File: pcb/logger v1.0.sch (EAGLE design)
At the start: 29 parts, among them J1 MICRO-SDCARD-CONNECTOR-330006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, K1 RESET, U1 DS1307ZN-1900100P1, U2 CJ1117-3.3-1310190P1, U3 74VHCT125PW, X1 32.768KHZ

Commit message: Mostly wired up
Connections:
- new net AREF: JP2.1, U$4.AREF
- new net D2: JP4.3, U$4.D2
- new net D3: JP4.4, U$4.*D3
- new net D4: JP4.5, U$4.D4
- new net D5: JP4.6, U$4.*D5
- new net D6: JP4.7, U$4.*D6
- new net D7: JP4.8, U$4.D7
- new net D8: JP2.8, U$4.D8
- new net D9: JP2.7, U$4.*D9
- new net N$55: U$4.SCL
- new net N$87: U$4.SDA
- new net RX: JP4.1, U$4.RX
- new net TX: JP4.2, U$4.TX
- net +3V3: now also U$4.3.3V
- net +5V: now also U$4.5V
- net GND: now also U$4.GND@0, U$4.GND@1, U$4.GND@2
- net MISO: now also U$4.D12
- net MOSI: now also U$4.*D11
- net RESET: now also U$4.RES
- net SCK: now also U$4.D13
- net SD_CS: now also U$4.*D10
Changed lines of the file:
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@@
 </variantdefs>
 <classes>
-<class number="0" name="default" width="0" drill="0">
+<class number="0" name="default" width="0.1524" drill="0.3302">
+</class>
+<class number="1" name="3V3" width="0.3048" drill="0.3302">
+<clearance class="0" value="0.1524"/>
+</class>
+<class number="2" name="5V" width="0.3048" drill="0.3302">
+<clearance class="0" value="0.1524"/>
+<clearance class="1" value="0.1524"/>
+</class>
+<class number="3" name="GND" width="0.1524" drill="0.3302">
+<clearance class="0" value="0.1524"/>
+<clearance class="1" value="0.1524"/>
+<clearance class="2" value="0.1524"/>
 </class>
 </classes>
@@
 </busses>
 <nets>
-<net name="+5V" class="0">
+<net name="+5V" class="2">
 <segment>
 <wire x1="53.34" y1="53.34" x2="53.34" y2="63.5" width="0.1524" layer="91"/>
@@
 <pinref part="P+2" gate="1" pin="+5V"/>
 <wire x1="43.18" y1="22.86" x2="44.45" y2="22.86" width="0.1524" layer="91"/>
-<junction x="45.72" y="22.86"/>
 <pinref part="U2" gate="U" pin="IN"/>
-<wire x1="44.45" y1="22.86" x2="45.72" y2="22.86" width="0.1524" layer="91"/>
-<junction x="44.45" y="22.86"/>
 </segment>
 <segment>
@@
 <pinref part="R8" gate="R" pin="2"/>
 </segment>
-</net>
-<net name="GND" class="0">
+<segment>
+<pinref part="U$4" gate="G$1" pin="5V"/>
+<wire x1="66.04" y1="83.82" x2="66.04" y2="76.2" width="0.1524" layer="91"/>
+<label x="66.04" y="76.2" size="1.778" layer="95" rot="R90"/>
+</segment>
+</net>
+<net name="GND" class="3">
 <segment>
 <wire x1="55.88" y1="55.88" x2="58.42" y2="55.88" width="0.1524" layer="91"/>
@@
 <pinref part="GND7" gate="1" pin="GND"/>
 <pinref part="JP2" gate="G$1" pin="2"/>
+<wire x1="40.64" y1="129.54" x2="40.64" y2="119.38" width="0.1524" layer="91"/>
+<junction x="40.64" y="129.54"/>
 </segment>
 <segment>
@@
 <pinref part="GND13" gate="1" pin="GND"/>
 <wire x1="147.32" y1="109.22" x2="147.32" y2="119.38" width="0.1524" layer="91"/>
+</segment>
+<segment>
+<pinref part="U$4" gate="G$1" pin="GND@2"/>
+<wire x1="73.66" y1="83.82" x2="73.66" y2="78.74" width="0.1524" layer="91"/>
+<pinref part="U$4" gate="G$1" pin="GND@0"/>
+<wire x1="78.74" y1="83.82" x2="78.74" y2="78.74" width="0.1524" layer="91"/>
+<wire x1="73.66" y1="78.74" x2="76.2" y2="78.74" width="0.1524" layer="91"/>
+<pinref part="U$4" gate="G$1" pin="GND@1"/>
+<wire x1="76.2" y1="78.74" x2="78.74" y2="78.74" width="0.1524" layer="91"/>
+<wire x1="76.2" y1="83.82" x2="76.2" y2="78.74" width="0.1524" layer="91"/>
+<junction x="76.2" y="78.74"/>
+<label x="73.66" y="76.2" size="1.778" layer="95"/>
 </segment>
 </net>
@@
 <pinref part="K1" gate="G$1" pin="A1"/>
 </segment>
-</net>
-<net name="+3V3" class="0">
+<segment>
+<pinref part="U$4" gate="G$1" pin="RES"/>
+<wire x1="60.96" y1="83.82" x2="60.96" y2="76.2" width="0.1524" layer="91"/>
+<label x="60.96" y="76.2" size="1.778" layer="95" rot="R90"/>
+</segment>
+</net>
+<net name="+3V3" class="1">
 <segment>
 <pinref part="JP12" gate="A" pin="1"/>
@@
 <pinref part="+3V2" gate="G$1" pin="+3V3"/>
 </segment>
+<segment>
+<pinref part="U$4" gate="G$1" pin="3.3V"/>
+<wire x1="68.58" y1="83.82" x2="68.58" y2="76.2" width="0.1524" layer="91"/>
+<label x="68.58" y="76.2" size="1.778" layer="95" rot="R90"/>
+</segment>
 </net>
 <net name="MOSI" class="0">
@@
 <pinref part="ICSP" gate="A" pin="4"/>
 <pinref part="JP2" gate="G$1" pin="5"/>
+<wire x1="48.26" y1="129.54" x2="48.26" y2="119.38" width="0.1524" layer="91"/>
+<junction x="48.26" y="129.54"/>
 </segment>
 <segment>
@@
 <label x="195.58" y="101.6" size="1.778" layer="95"/>
 <pinref part="JP1" gate="A" pin="2"/>
+</segment>
+<segment>
+<pinref part="U$4" gate="G$1" pin="*D11"/>
+<wire x1="68.58" y1="109.22" x2="68.58" y2="114.3" width="0.1524" layer="91"/>
 </segment>
 </net>
@@
 <pinref part="ICSP" gate="A" pin="1"/>
 <pinref part="JP2" gate="G$1" pin="4"/>
+<wire x1="45.72" y1="129.54" x2="45.72" y2="119.38" width="0.1524" layer="91"/>
+<junction x="45.72" y="129.54"/>
 </segment>
 <segment>
@@
 <wire x1="124.46" y1="88.9" x2="134.62" y2="88.9" width="0.1524" layer="91"/>
 <wire x1="134.62" y1="88.9" x2="134.62" y2="93.98" width="0.1524" layer="91"/>
+</segment>
+<segment>
+<pinref part="U$4" gate="G$1" pin="D12"/>
+<wire x1="71.12" y1="109.22" x2="71.12" y2="114.3" width="0.1524" layer="91"/>
 </segment>
 </net>
@@
 <pinref part="ICSP" gate="A" pin="3"/>
 <pinref part="JP2" gate="G$1" pin="3"/>
+<wire x1="43.18" y1="129.54" x2="43.18" y2="119.38" width="0.1524" layer="91"/>
+<junction x="43.18" y="129.54"/>
 </segment>
 <segment>
@@
 <label x="195.58" y="96.52" size="1.778" layer="95"/>
 <pinref part="JP1" gate="A" pin="4"/>
+</segment>
+<segment>
+<pinref part="U$4" gate="G$1" pin="D13"/>
+<wire x1="73.66" y1="109.22" x2="73.66" y2="114.3" width="0.1524" layer="91"/>
 </segment>
 </net>
@@
 <label x="60.96" y="144.78" size="1.778" layer="95" rot="MR0"/>
 <pinref part="JP2" gate="G$1" pin="6"/>
+<wire x1="50.8" y1="129.54" x2="50.8" y2="119.38" width="0.1524" layer="91"/>
+<junction x="50.8" y="129.54"/>
+</segment>
+<segment>
+<pinref part="U$4" gate="G$1" pin="*D10"/>
+<wire x1="66.04" y1="109.22" x2="66.04" y2="114.3" width="0.1524" layer="91"/>
 </segment>
 </net>
@@
 </segment>
 </net>
+<net name="N$55" class="0">
+<segment>
+<pinref part="U$4" gate="G$1" pin="SCL"/>
+<wire x1="78.74" y1="109.22" x2="78.74" y2="114.3" width="0.1524" layer="91"/>
+</segment>
+</net>
+<net name="N$87" class="0">
+<segment>
+<pinref part="U$4" gate="G$1" pin="SDA"/>
+<wire x1="76.2" y1="109.22" x2="76.2" y2="114.3" width="0.1524" layer="91"/>
+</segment>
+</net>
+<net name="D9" class="0">
+<segment>
+<pinref part="U$4" gate="G$1" pin="*D9"/>
+<wire x1="63.5" y1="109.22" x2="63.5" y2="114.3" width="0.1524" layer="91"/>
+</segment>
+<segment>
+<pinref part="JP2" gate="G$1" pin="7"/>
+<wire x1="53.34" y1="129.54" x2="53.34" y2="119.38" width="0.1524" layer="91"/>
+</segment>
+</net>
+<net name="D8" class="0">
+<segment>
+<pinref part="U$4" gate="G$1" pin="D8"/>
+<wire x1="60.96" y1="109.22" x2="60.96" y2="114.3" width="0.1524" layer="91"/>
+</segment>
+<segment>
+<pinref part="JP2" gate="G$1" pin="8"/>
+<wire x1="55.88" y1="129.54" x2="55.88" y2="119.38" width="0.1524" layer="91"/>
+</segment>
+</net>
+<net name="D7" class="0">
+<segment>
+<pinref part="U$4" gate="G$1" pin="D7"/>
+<wire x1="58.42" y1="109.22" x2="58.42" y2="114.3" width="0.1524" layer="91"/>
+</segment>
+<segment>
+<pinref part="JP4" gate="G$1" pin="8"/>
+<wire x1="63.5" y1="129.54" x2="63.5" y2="119.38" width="0.1524" layer="91"/>
+</segment>
+</net>
+<net name="D6" class="0">
+<segment>
+<pinref part="U$4" gate="G$1" pin="*D6"/>
+<wire x1="55.88" y1="109.22" x2="55.88" y2="114.3" width="0.1524" layer="91"/>
+</segment>
+<segment>
+<pinref part="JP4" gate="G$1" pin="7"/>
+<wire x1="66.04" y1="129.54" x2="66.04" y2="119.38" width="0.1524" layer="91"/>
+</segment>
+</net>
+<net name="D5" class="0">
+<segment>
+<pinref part="U$4" gate="G$1" pin="*D5"/>
+<wire x1="53.34" y1="109.22" x2="53.34" y2="114.3" width="0.1524" layer="91"/>
+</segment>
+<segment>
+<pinref part="JP4" gate="G$1" pin="6"/>
+<wire x1="68.58" y1="129.54" x2="68.58" y2="119.38" width="0.1524" layer="91"/>
+</segment>
+</net>
+<net name="D4" class="0">
+<segment>
+<pinref part="U$4" gate="G$1" pin="D4"/>
+<wire x1="50.8" y1="109.22" x2="50.8" y2="114.3" width="0.1524" layer="91"/>
+</segment>
+<segment>
+<pinref part="JP4" gate="G$1" pin="5"/>
+<wire x1="71.12" y1="129.54" x2="71.12" y2="119.38" width="0.1524" layer="91"/>
+</segment>
+</net>
+<net name="D3" class="0">
+<segment>
+<pinref part="U$4" gate="G$1" pin="*D3"/>
+<wire x1="48.26" y1="109.22" x2="48.26" y2="114.3" width="0.1524" layer="91"/>
+</segment>
+<segment>
+<pinref part="JP4" gate="G$1" pin="4"/>
+<wire x1="73.66" y1="129.54" x2="73.66" y2="119.38" width="0.1524" layer="91"/>
+</segment>
+</net>
+<net name="D2" class="0">
+<segment>
+<pinref part="U$4" gate="G$1" pin="D2"/>
+<wire x1="45.72" y1="109.22" x2="45.72" y2="114.3" width="0.1524" layer="91"/>
+</segment>
+<segment>
+<pinref part="JP4" gate="G$1" pin="3"/>
+<wire x1="76.2" y1="129.54" x2="76.2" y2="119.38" width="0.1524" layer="91"/>
+</segment>
+</net>
+<net name="TX" class="0">
+<segment>
+<pinref part="U$4" gate="G$1" pin="TX"/>
+<wire x1="40.64" y1="109.22" x2="40.64" y2="114.3" width="0.1524" layer="91"/>
+</segment>
+<segment>
+<pinref part="JP4" gate="G$1" pin="2"/>
+<wire x1="78.74" y1="129.54" x2="78.74" y2="119.38" width="0.1524" layer="91"/>
+</segment>
+</net>
+<net name="RX" class="0">
+<segment>
+<pinref part="U$4" gate="G$1" pin="RX"/>
+<wire x1="38.1" y1="109.22" x2="38.1" y2="114.3" width="0.1524" layer="91"/>
+</segment>
+<segment>
+<pinref part="JP4" gate="G$1" pin="1"/>
+<wire x1="81.28" y1="129.54" x2="81.28" y2="119.38" width="0.1524" layer="91"/>
+</segment>
+</net>
+<net name="AREF" class="3">
+<segment>
+<pinref part="JP2" gate="G$1" pin="1"/>
+<wire x1="38.1" y1="129.54" x2="38.1" y2="119.38" width="0.1524" layer="91"/>
+</segment>
+<segment>
+<pinref part="U$4" gate="G$1" pin="AREF"/>
+<wire x1="71.12" y1="83.82" x2="71.12" y2="76.2" width="0.1524" layer="91"/>
+</segment>
+</net>

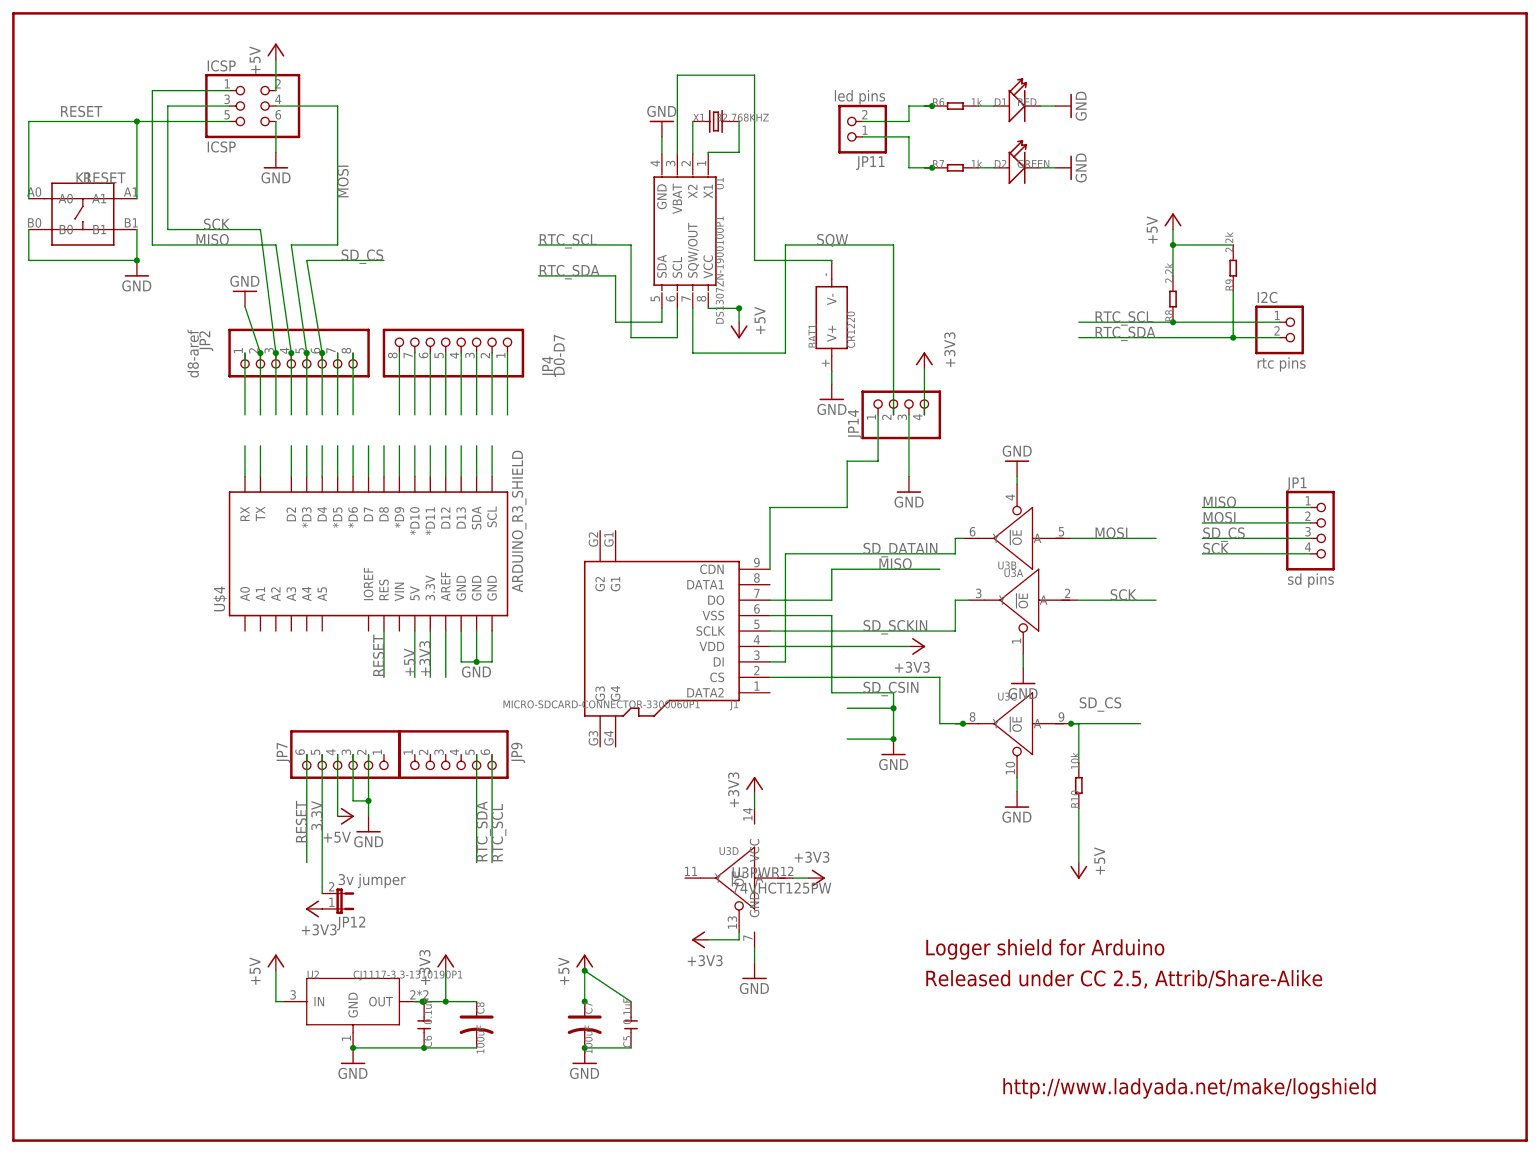
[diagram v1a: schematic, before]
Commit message: Added extra LED's, finished wiring
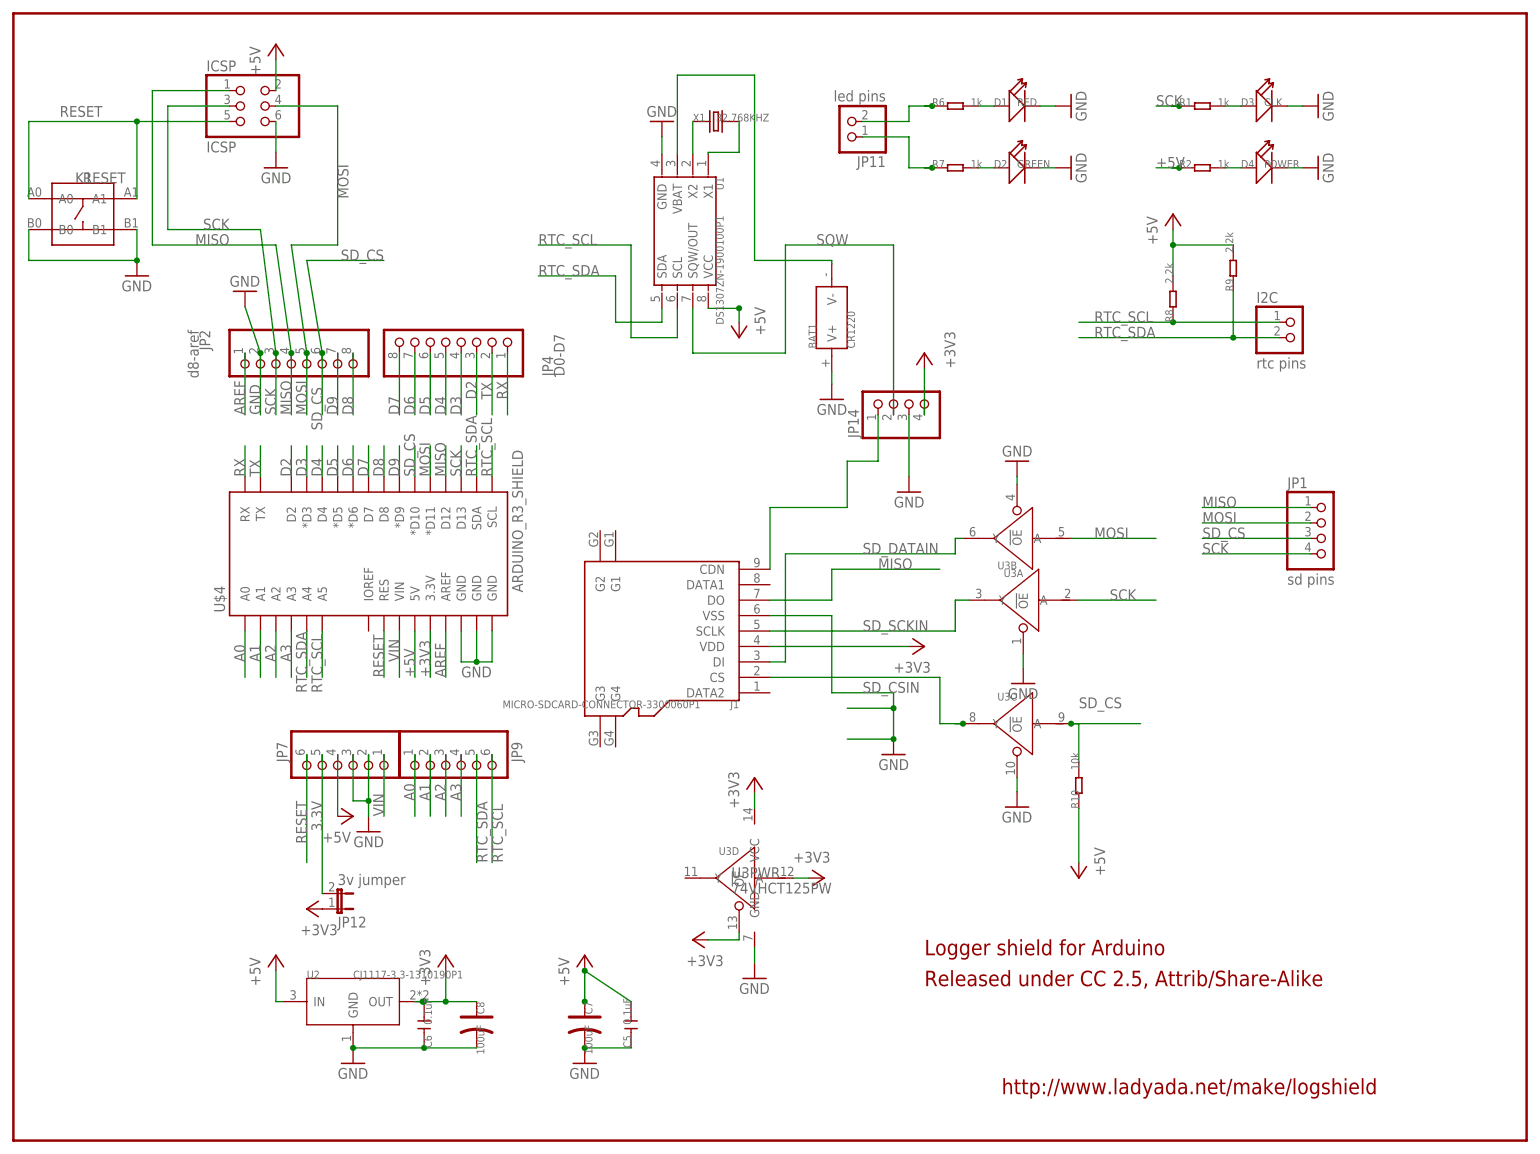
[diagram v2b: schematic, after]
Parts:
- added D3: CLK, Discrete:LED'0603'
- added D4: POWER, Discrete:LED'0603'
- added R1, R2: 1k, Discrete:R-0603
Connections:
- removed net N$55: U$4.SCL
- removed net N$87: U$4.SDA
- new net A0: JP9.1, U$4.A0
- new net A1: JP9.2, U$4.A1
- new net A2: JP9.3, U$4.A2
- new net A3: JP9.4, U$4.A3
- new net N$26: D3.+, R1.2
- new net N$40: D4.+, R2.2
- new net VIN: JP7.1, U$4.VIN
- net +5V: now also R2.1
- net GND: now also D3.-, D4.-
- net RTC_SCL: now also U$4.A5, U$4.SCL
- net RTC_SDA: now also U$4.A4, U$4.SDA
- net SCK: now also R1.1
